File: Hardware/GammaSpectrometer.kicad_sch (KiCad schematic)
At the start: 0 parts

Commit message: fix: #145, fix: #159
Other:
- added sheet PowerInput (PowerInput.kicad_sch)
- sheet AnalogPowerNegative ports: added VIN; removed none
- sheet AnalogPowerPositive ports: added VIN; removed none
- sheet FPGA ports: added VCC_2V5, {FPGA_CFG_IF}; removed none
- sheet FPGAConfiguration ports: added VCC_3V3, {FPGA_CFG_IF}; removed none
- sheet SiPMBiasRegulator ports: added VIN; removed none
- company: (none) -> RG
- title: (none) -> Top-Level System Architecture

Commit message: fix: #160, fix: #163, fix: #164
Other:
- sheet ClockGeneration renamed Clock Generation
- sheet DigitalPower renamed Digital Power
- sheet FPGAConfiguration renamed FPGA Configuration
- sheet PowerInput renamed Power Input
- removed sheet AnalogPowerNegative
- removed sheet AnalogPowerPositive
- removed sheet SiPMBiasControl
- removed sheet SiPMBiasRegulator
- removed sheet SiPMOverlightProtection
- added sheet Analog Power (AnalogPower.kicad_sch)
- added sheet SiPM Bias (SiPMBias.kicad_sch)
- added sheet Vref 2v048 (Vref2V048.kicad_sch)
- sheet ADC ports: added +2V048_VREF, +3V3_ADC, +5V0_ADC, AFE_OUT_N, AFE_OUT_P; removed ADC_REF, VCC_3V3, VCC_5V, {SIPM_ADC}
- sheet AFE ports: added +2V048_VREF, +2V5_AFE, +5V0_AFE, -2V5_AFE, -5V0_AFE, AFE_OUT_N, AFE_OUT_P; removed ADC_REF, VCC_2V5, VCC_5V, VEE_2V5, VEE_5V, {SIPM_ADC}
- sheet Clock Generation ports: added +3V3_CLKGEN; removed VCC_3V3_CLK
- sheet Digital Power ports: added +1V2_D, +2V5_D, +3V3_CLKGEN, +3V3_D, +V_IN; removed VCC_1V2, VCC_3V3, VCC_3V3_CLK, VCC_5V, VIN
- sheet FPGA ports: added +1V2_FPGA, +2V5_FPGA, +3V3_FPGA, SIPM_BIAS_OK, {SIPM_BIAS_I2C}; removed SIPM_EN, SIPM_OVERLIGHT_FAULT, VCC_1V2, VCC_2V5, VCC_3V3
- sheet FPGA Configuration ports: added +3V3_D; removed VCC_3V3
- sheet Power Input ports: added +V_IN; removed VIN

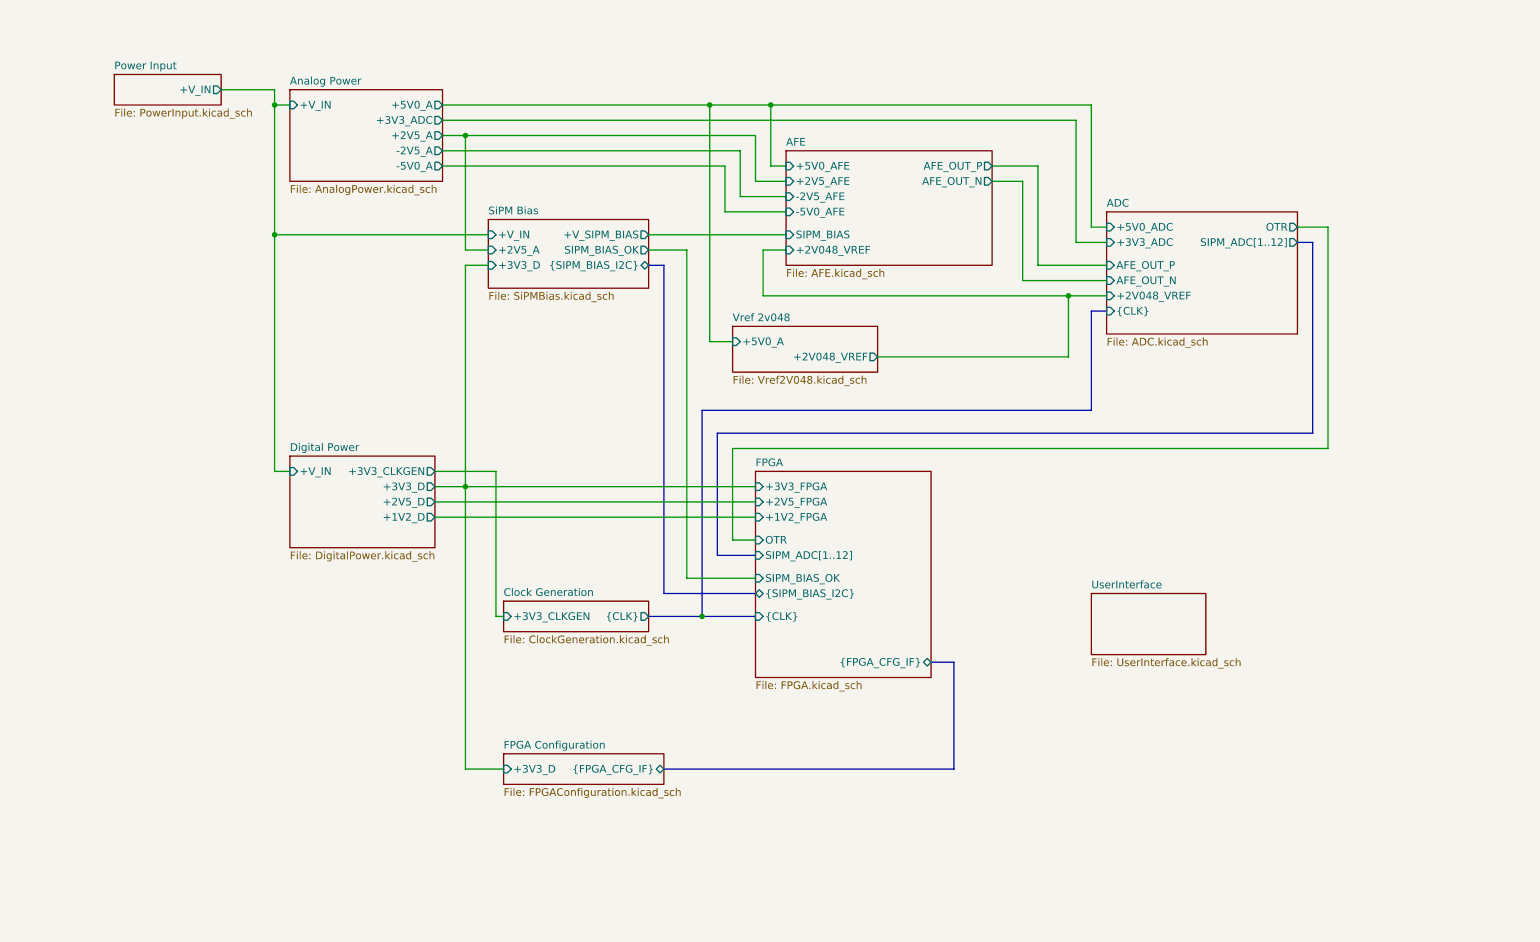
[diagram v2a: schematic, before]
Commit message: fix: #134
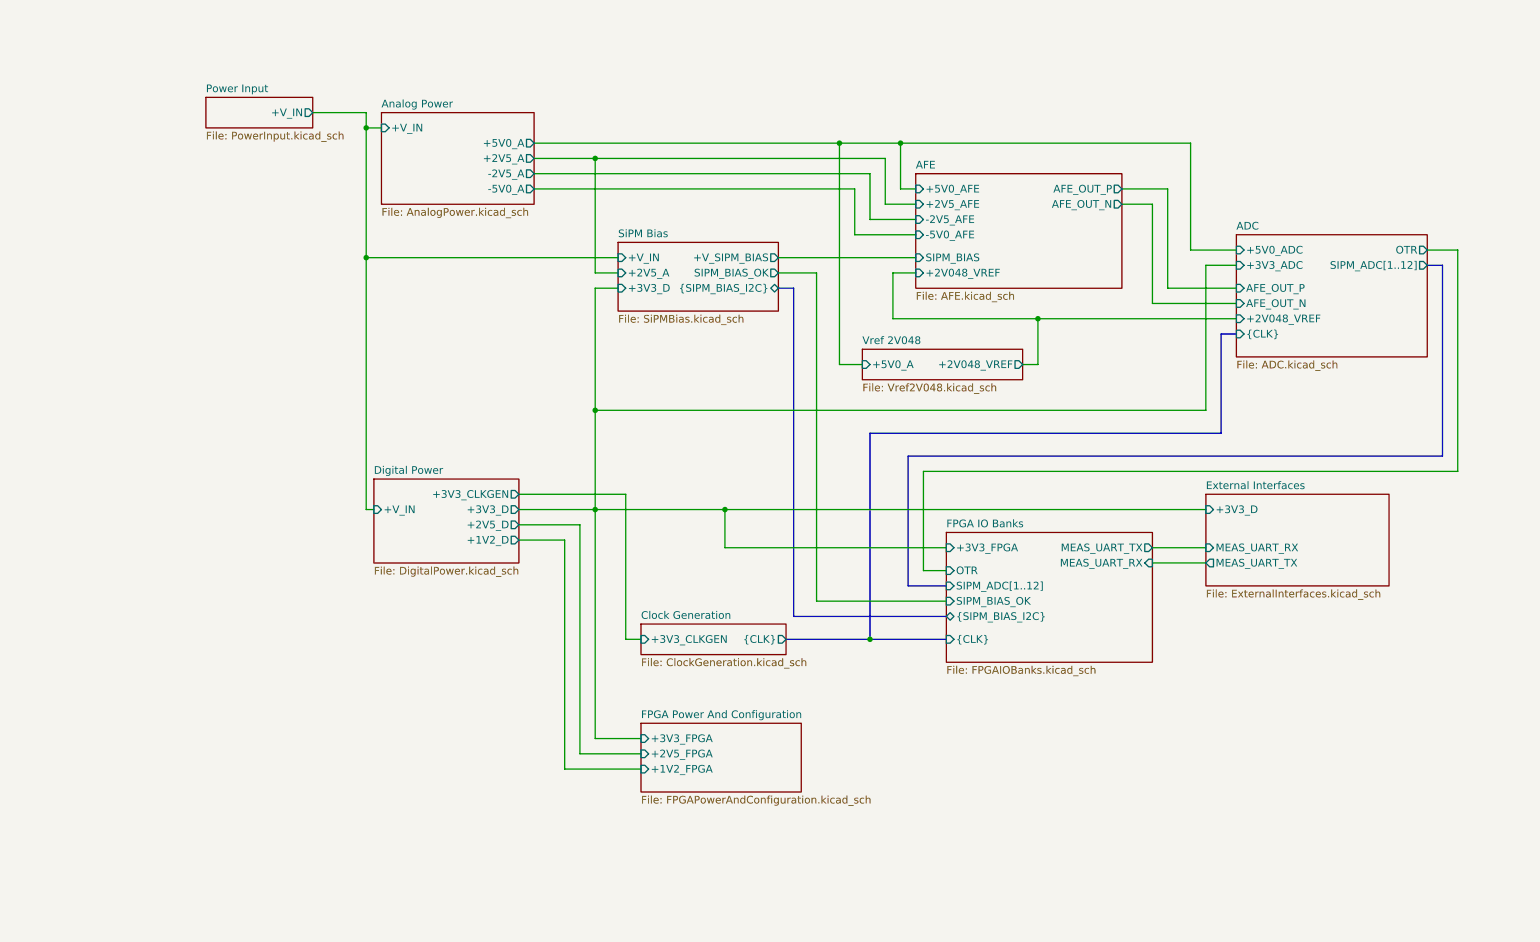
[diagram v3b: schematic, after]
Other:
- sheet FPGA renamed FPGA IO Banks
- sheet FPGA Configuration renamed FPGA Power And Configuration
- sheet Vref 2v048 renamed Vref 2V048
- removed sheet UserInterface
- added sheet External Interfaces (ExternalInterfaces.kicad_sch)
- sheet Analog Power ports: added none; removed +3V3_ADC
- sheet FPGA IO Banks: file FPGA.kicad_sch -> FPGAIOBanks.kicad_sch
- sheet FPGA IO Banks ports: added MEAS_UART_RX, MEAS_UART_TX; removed +1V2_FPGA, +2V5_FPGA, {FPGA_CFG_IF}
- sheet FPGA Power And Configuration: file FPGAConfiguration.kicad_sch -> FPGAPowerAndConfiguration.kicad_sch
- sheet FPGA Power And Configuration ports: added +1V2_FPGA, +2V5_FPGA, +3V3_FPGA; removed +3V3_D, {FPGA_CFG_IF}

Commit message: fix: #170, fix: #144, fix: #132
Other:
- removed sheet FPGA IO Banks
- removed sheet Vref 2V048
- added sheet FPGA IO Banks 0-1 (FPGAIOBanks01.kicad_sch)
- added sheet FPGA IO Banks 2-3 (FPGAIOBanks23.kicad_sch)
- sheet ADC ports: added +3V3_A, +3V3_D, AFE_OUT_CH1_N, AFE_OUT_CH1_P, AFE_OUT_CH2_N, AFE_OUT_CH2_P, SIPM_ADC_CH1_DATA[1..12], SIPM_ADC_CH1_OTR, SIPM_ADC_CH2_DATA[1..12], SIPM_ADC_CH2_OTR, {SIPM_ADC_CFG_IF}; removed +2V048_VREF, +3V3_ADC, +5V0_ADC, AFE_OUT_N, AFE_OUT_P, OTR, SIPM_ADC[1..12], {CLK}
- sheet AFE ports: added +3V3_A, -3V3_A, AFE_CH1_N, AFE_CH1_P, AFE_CH2_N, AFE_CH2_P; removed +2V048_VREF, +2V5_AFE, +5V0_AFE, -2V5_AFE, -5V0_AFE, AFE_OUT_N, AFE_OUT_P
- sheet Analog Power ports: added +3V3_A, -3V3_A; removed +2V5_A, +5V0_A, -2V5_A, -5V0_A
- sheet SiPM Bias ports: added +3V3_A; removed +2V5_A
- note added: "Add Signal Domain Color Coding (Optional but pro) Some teams: Use green for power Blue for high-speed Orange for control"
- note added: "At 65 MSPS, 12-bit parallel bus: Are you using series termination? Is FPGA bank voltage matching DRVDD? Is IO standard LVTTL 3.3 V? Is timing margin analyzed? Even if handled in sub-sheets, the system sheet should imply interface class."
- note added: "System Design Notes: • Analog and digital grounds joined at single star point under ADC. • +3V3_A generated via low-noise LDO (TPS7A47) from +V_IN. • +3V3_D derived from digital buck regulator. • +3V3_CLKGEN isolated via ferrite bead from +3V3_D. • ADC digital IO operates at 3.3V LVCMOS. • Clock jitter target < 1ps RMS."
